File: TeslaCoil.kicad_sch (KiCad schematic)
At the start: 32 parts, among them J1 Screw_Terminal_01x03, J2 Screw_Terminal_01x02, Q1 Q_NIGBT_GCE, Q2 Q_NIGBT_GCE, Q3 Q_NIGBT_GCE, Q4 Q_NIGBT_GCE

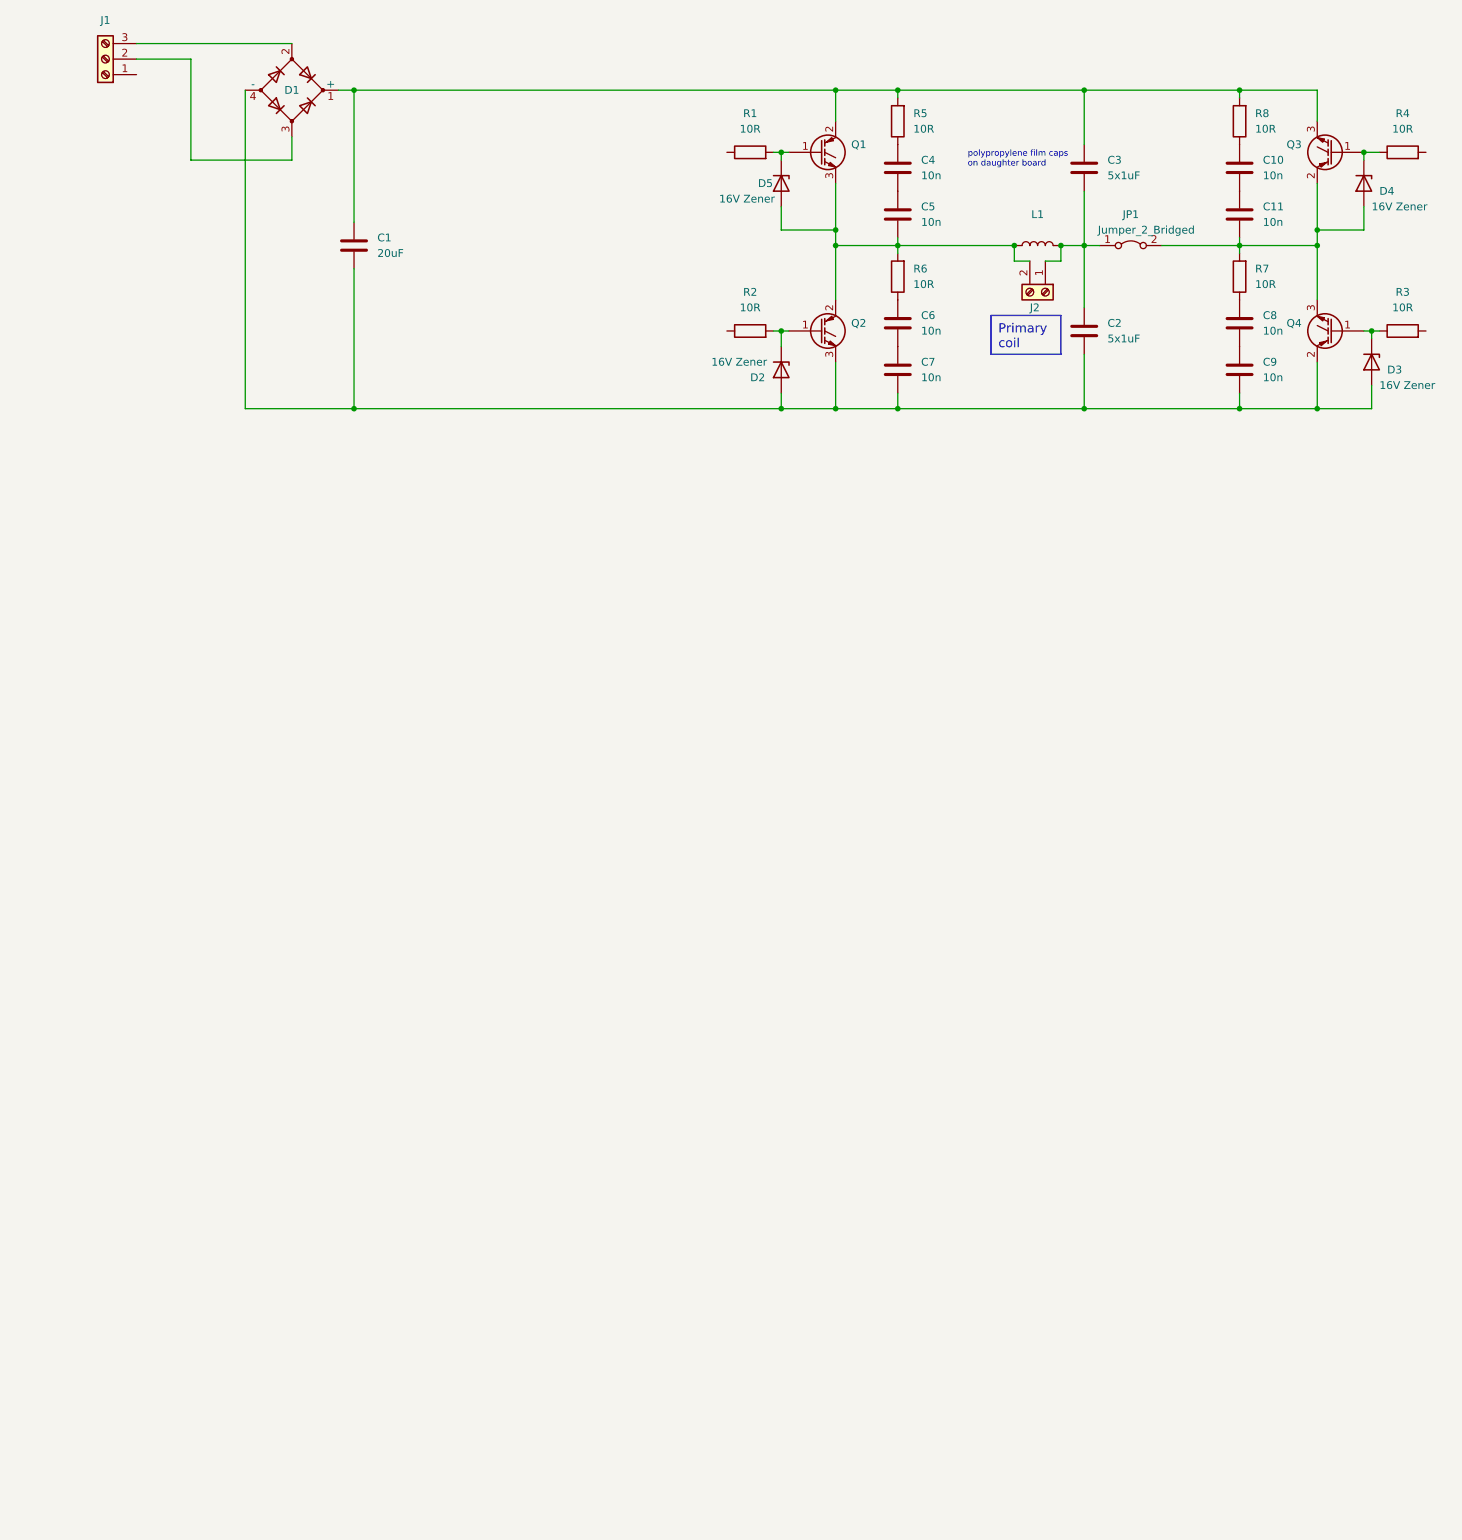
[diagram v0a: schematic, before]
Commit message: add gate driver
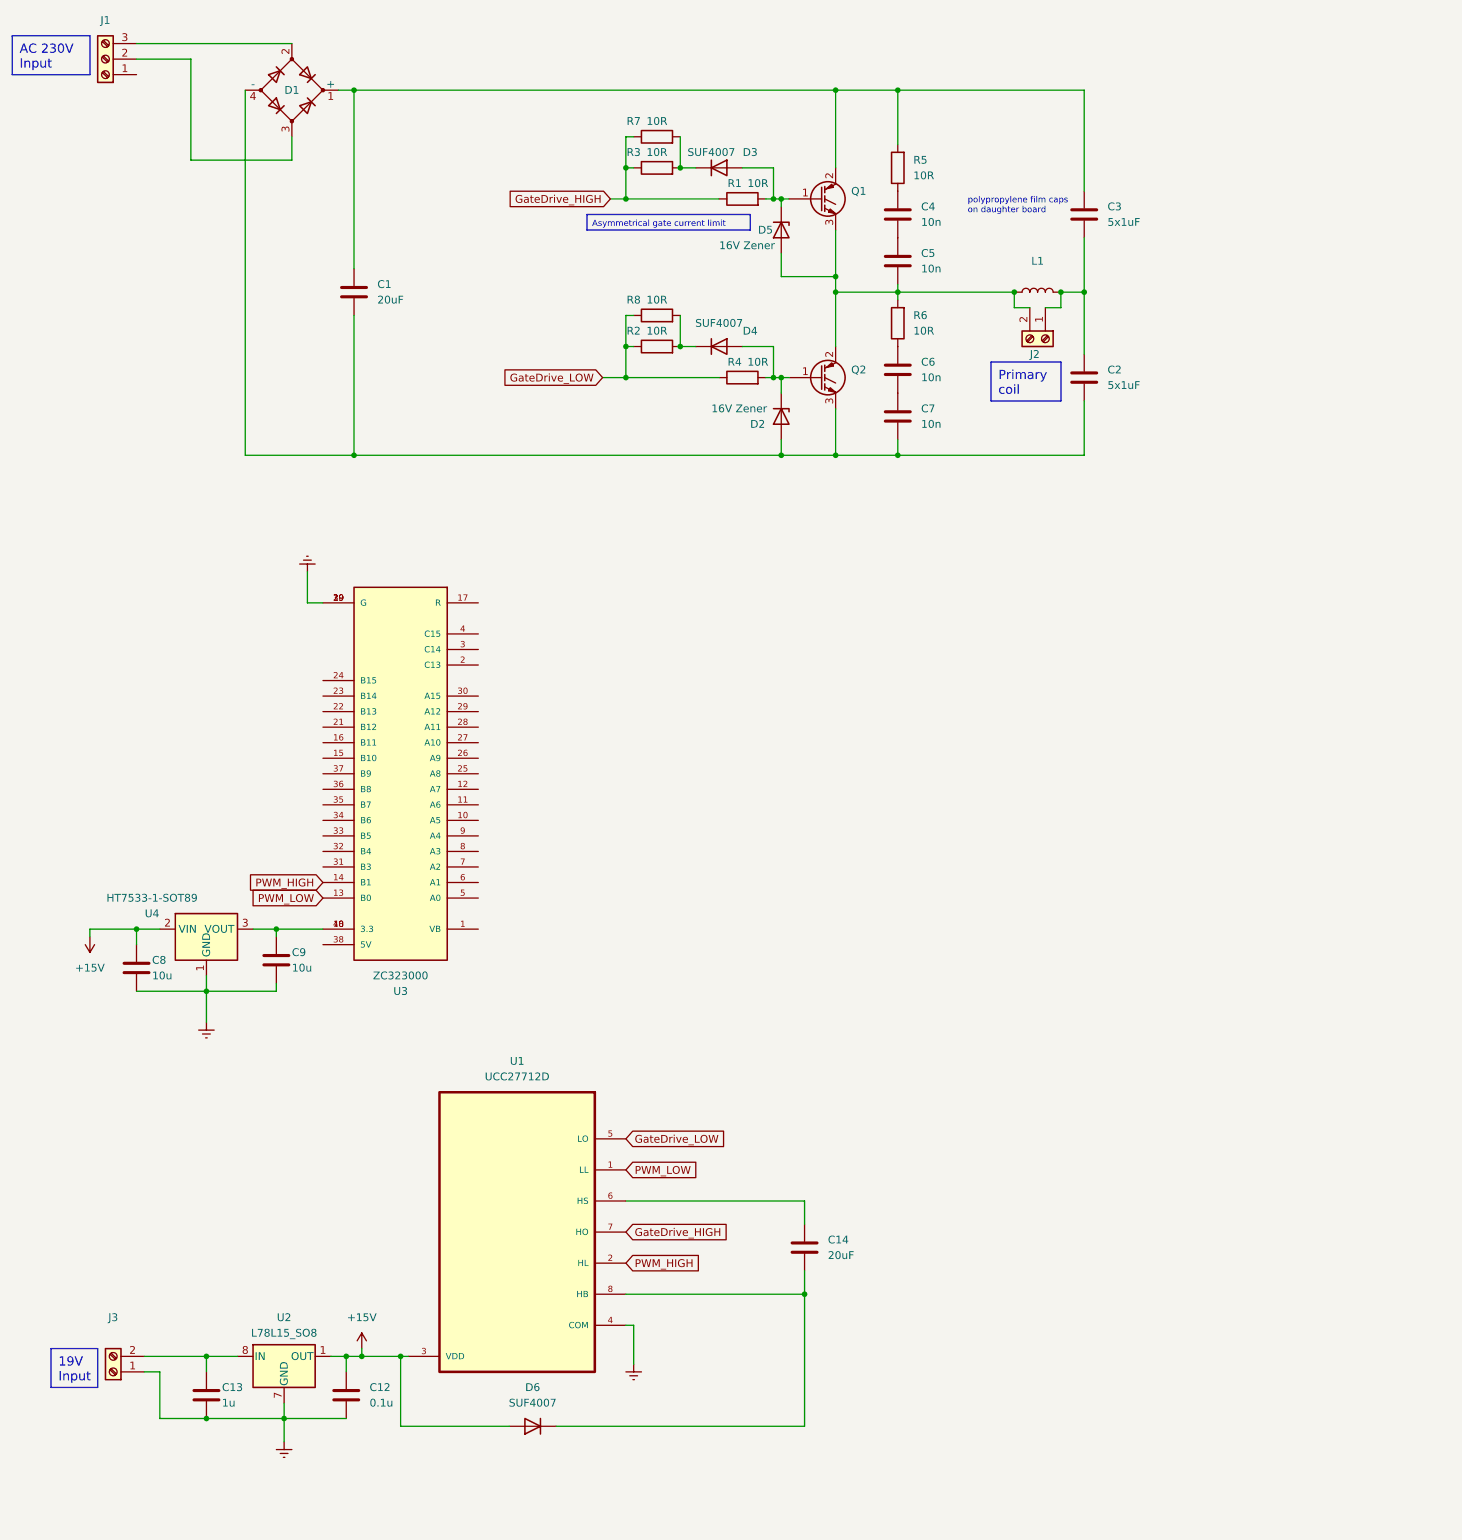
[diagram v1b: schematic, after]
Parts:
- removed C10, C11: 10n, symbol Device:C
- removed D3, D4: 16V Zener, symbol Device:D_Zener
- removed JP1: Jumper_2_Bridged, symbol Jumper:Jumper_2_Bridged
- removed Q3, Q4: Q_NIGBT_GCE, symbol Device:Q_NIGBT_GCE
- added C12: 0.1u, symbol Device:C
- added C13: 1u, symbol Device:C
- added C14: 20uF, symbol Device:C
- added D3, D4, D6: SUF4007, Diode_SMD:D_MELF_Handsoldering, symbol Diode:SM516
- added J3: Screw_Terminal_01x02, symbol Connector:Screw_Terminal_01x02
- added U1: UCC27712D, Snapeda:UCC27712D_SOIC127P599X175-8N, symbol Snapeda_kicad_sym:UCC27712D
- added U2: L78L15_SO8, Package_SO:SOIC-8_3.9x4.9mm_P1.27mm, symbol Regulator_Linear:L78L15_SO8
- added U3: ZC323000, Snapeda:ZC323000_MODULE_ZC323000, symbol Snapeda_kicad_sym:ZC323000
- added U4: HT7533-1-SOT89, Package_TO_SOT_SMD:SOT-89-3, symbol Regulator_Linear:HT75xx-1-SOT89
- C8, C9: value 10n -> 10u
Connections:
- net at C1.1, C3.1, D1.1 (+)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: no longer R8.2
- net at C1.2, C2.2, C7.2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: no longer C9.2
- net +15V: now reaches C8.1
- net +15V: now also C12.1, D6.2 (A), U1.3 (VDD), U2.1 (OUT), U4.2 (VIN); no longer R7.1
- net at C9.1: now also U3.18 (3.3), U3.40 (3.3), U4.3 (VOUT); no longer C8.2
- net GateDrive_HIGH: now reaches R3.1
- net GateDrive_HIGH: now also R1.1, R7.1, U1.7 (HO)
- net at R7.2: now also R3.2, D3.1 (K)
- net GateDrive_LOW: now reaches R2.1
- net GateDrive_LOW: now also R4.1, R8.1, U1.5 (LO)
- net at D2.1 (K), Q2.1 (G): now also R4.2, D4.2 (A); no longer R2.2
- net at D5.1 (K), Q1.1 (G), R1.2: now also D3.2 (A)
- new net: C13.1, J3.2 (Pin_2), U2.8 (IN)
- new net: D4.1 (K), R2.2, R8.2
- new net: C14.2, D6.1 (K), U1.8 (HB)
- new net: C14.1, U1.6 (HS)
- new net Earth: C12.2, C13.2, C8.2, C9.2, J3.1 (Pin_1), U1.4 (COM), U2.2 (GND), U2.3 (GND), U2.6 (GND), U2.7 (GND), U3.19 (G), U3.20 (G), U3.39 (G), U4.1 (GND)
- new net PWM_HIGH: U1.2 (HL), U3.14 (B1)
- new net PWM_LOW: U1.1 (LL), U3.13 (B0)
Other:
- moved on the sheet: C1, C2, C3, C4, C5, C6, C7, D2, D5, J2, L1, Q1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

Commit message: footprints
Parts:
- removed D1: D_Bridge_+AA-, symbol Device:D_Bridge_+AA-
- added D1: GBJ1008-BP, Snapeda:GBJ1008-BP_DIOB_GBJ1008-BP, symbol Snapeda_kicad_sym:GBJ1008-BP
- C1: footprint (none) -> Capacitor_THT:CP_Radial_D17.0mm_P7.50mm
- C12, C13, C14, C8, C9: footprint (none) -> Capacitor_SMD:C_0805_2012Metric_Pad1.18x1.45mm_HandSolder
- C2, C3: footprint (none) -> Capacitor_THT:C_Rect_L18.0mm_W5.0mm_P15.00mm_FKS3_FKP3
- C4, C5, C6, C7: footprint (none) -> Capacitor_THT:C_Rect_L13.0mm_W5.0mm_P10.00mm_FKS3_FKP3_MKS4
- D2, D5: footprint (none) -> Diode_SMD:D_0805_2012Metric
- J1: footprint (none) -> TerminalBlock_4Ucon:TerminalBlock_4Ucon_1x03_P3.50mm_Horizontal
- J2, J3: footprint (none) -> TerminalBlock_4Ucon:TerminalBlock_4Ucon_1x02_P3.50mm_Horizontal
- Q1, Q2: footprint (none) -> Package_TO_SOT_THT:TO-247-3_Vertical
- R1, R2, R3, R4, R7, R8: footprint (none) -> Resistor_SMD:R_0603_1608Metric_Pad0.98x0.95mm_HandSolder
- R5, R6: footprint (none) -> Resistor_THT:R_Axial_Power_L25.0mm_W9.0mm_P10.16mm_Vertical
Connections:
- net at C1.1, C3.1, Q1.2 (C)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: now also D1.4
- net at C1.2, C2.2, C7.2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: now also D1.1
- net at J1.2 (Pin_2): now also D1.3
- net at J1.3 (Pin_3): now also D1.2

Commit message: layout mockup
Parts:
- added D7, D8: SUF4007, Diode_SMD:D_MELF_Handsoldering, symbol Diode:SM516
- added L2: AS101, Snapeda:ASM-010_ASM-010, symbol Snapeda_kicad_sym:ASM-010
- added R10, R9: 100k, Resistor_THT:R_Axial_DIN0207_L6.3mm_D2.5mm_P7.62mm_Horizontal, symbol Device:R
- added R11: 1k, Resistor_THT:R_Axial_DIN0207_L6.3mm_D2.5mm_P7.62mm_Horizontal, symbol Device:R
- added SW1: SW_SPST, symbol Switch:SW_SPST
- added TP1: Current transformer wire, TestPoint:TestPoint_Bridge_Pitch7.62mm_Drill1.3mm, symbol Connector:TestPoint_2Pole
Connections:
- net Earth: now also D8.2 (A), L2.P$1
- net at C1.2, C2.2, C7.2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: now also R10.2
- net at D1.2: now also SW1.2 (B); no longer J1.3 (Pin_3)
- net at C1.1, C3.1, D1.4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: now also R9.1
- net +3.3V: now reaches C9.1, U3.18 (3.3), U3.40 (3.3), U4.3 (VOUT)
- net +3.3V: now also D7.1 (K)
- net at J2.1 (Pin_1), L1.2: now also TP1.1; no longer C2.1, C3.2
- net Current Sense: now reaches U3.6 (A1)
- net Current Sense: now also D7.2 (A), D8.1 (K), R11.2
- new net: L2.P$2, R11.1
- new net: C2.1, C3.2, R10.1, R9.2, TP1.2
- new net: J1.3 (Pin_3), SW1.1 (A)
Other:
- moved on the sheet: C2, C3, U3

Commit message: layout 2nd rev
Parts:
- removed C1: 20uF, Capacitor_THT:CP_Radial_D17.0mm_P7.50mm, symbol Device:C
- removed D2, D5: 16V Zener, Diode_SMD:D_0805_2012Metric, symbol Device:D_Zener
- removed D7, D8: SUF4007, Diode_SMD:D_MELF_Handsoldering, symbol Diode:SM516
- removed L2: AS101, Snapeda:ASM-010_ASM-010, symbol Snapeda_kicad_sym:ASM-010
- removed TP1: Current transformer wire, TestPoint:TestPoint_Bridge_Pitch7.62mm_Drill1.3mm, symbol Connector:TestPoint_2Pole
- removed U2: L78L15_SO8, Package_SO:SOIC-8_3.9x4.9mm_P1.27mm, symbol Regulator_Linear:L78L15_SO8
- added C1, C10, C11, C15: 220uF, Capacitor_THT:CP_Radial_D22.0mm_P10.00mm_SnapIn, symbol Device:C_Polarized_US
- added C16: 4x100nF, Capacitor_SMD:C_0603_1608Metric, symbol Device:C
- added D2, D5, D7: LED, LED_SMD:LED_0805_2012Metric, symbol Device:LED
- added J4: MCSP-Q-08-A-SG-T_R, Samacsys:MCSPQ08ASGTR, symbol Samacsys_kicad_sym:MCSP-Q-08-A-SG-T_R
- added JP1, JP2, JP3, JP4, JP5, JP6, JP7, JP8: Solder Jumper, Jumper:SolderJumper-2_P1.3mm_Open_TrianglePad1.0x1.5mm, symbol Jumper:SolderJumper_2_Open
- added R12, R14, R15, R18, R19: 1k, Resistor_SMD:R_0603_1608Metric_Pad0.98x0.95mm_HandSolder, symbol Device:R
- added R13: 10k, Resistor_SMD:R_0603_1608Metric_Pad0.98x0.95mm_HandSolder, symbol Device:R
- added R16, R17: 10R, Resistor_SMD:R_0603_1608Metric_Pad0.98x0.95mm_HandSolder, symbol Device:R
- added RV1: 10k pot, Snapeda:potentiometer, symbol Device:R_Potentiometer
- added T1: Gate drive transformer, Transformer_THT:Transformer_Toroid_Tapped_Horizontal_D10.5mm_Amidon-T37, symbol Device:Transformer_1P_2S
- added U2: LM317_TO-220, Package_TO_SOT_THT:TO-220-3_Vertical, symbol Regulator_Linear:LM317_TO-220
- C12: value 0.1u -> 100nF; footprint Capacitor_SMD:C_0805_2012Metric_Pad1.18x1.45mm_HandSolder -> Capacitor_SMD:C_0603_1608Metric
- C13: value 1u -> 100nF; footprint Capacitor_SMD:C_0805_2012Metric_Pad1.18x1.45mm_HandSolder -> Capacitor_SMD:C_0603_1608Metric
- C14: value 20uF -> 100nF; footprint Capacitor_SMD:C_0805_2012Metric_Pad1.18x1.45mm_HandSolder -> Capacitor_SMD:C_0603_1608Metric
- R11: footprint Resistor_THT:R_Axial_DIN0207_L6.3mm_D2.5mm_P7.62mm_Horizontal -> Resistor_SMD:R_0603_1608Metric_Pad0.98x0.95mm_HandSolder
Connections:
- net +15V: now also D7.2 (A), R12.2, U2.2 (VO); no longer C12.1, D6.2 (A), U1.3 (VDD)
- net +3.3V: now also J4.4 (VDD), RV1.3
- net Earth: now also R11.1, J4.6 (VSS), J4.MP1, J4.MP2, J4.MP3, J4.MP4, JP7.2 (B), JP8.1 (A), R14.1, R15.1, R19.1, RV1.1; no longer C12.2, C13.2
- net PWM_HIGH: now also U3.13 (B0), R16.2; no longer U1.2 (HL), U3.14 (B1)
- net PWM_LOW: now also U3.14 (B1), R17.2; no longer U1.1 (LL), U3.13 (B0)
- net at J3.2 (Pin_2): now also U2.3 (VI); no longer C13.1
- net Bridge_Low: now reaches C2.2, C7.2, D1.1, Q2.3 (E), R10.2
- net Bridge_Low: now also C10.2, C15.2, JP8.2 (B), T1.6 (SD)
- net at C3.1, D1.4, Q1.2 (C)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: now also C1.1, C11.1
- net Bridge_Midpoint: now reaches C5.2, J2.2 (Pin_2), L1.1, Q1.3 (E), Q2.2 (C), R6.2
- net Bridge_Midpoint: now also JP6.2 (B), T1.4 (SB)
- net at C14.2, D6.1 (K), U1.8 (HB): now also C12.2, C13.2, C16.2
- net at C14.1, U1.6 (HS): now also C12.1, C13.1, C16.1, JP6.1 (A), JP7.1 (A)
- net at J2.1 (Pin_1), L1.2: now also C2.1, C3.2, R10.1, R9.2, C1.2, C10.1, C11.2, C15.1
- net at U3.10 (A5): now also J4.5 (CLX)
- net at U3.11 (A6): now also J4.7 (DAT0)
- net at U3.12 (A7): now also J4.3 (CMD)
- net at U3.15 (B10): now also D2.2 (A)
- net at U3.16 (B11): now also D5.2 (A)
- net at U3.9 (A4): now also J4.2 (CD/DAT3)
- net Current Sense: no longer names the net of U3.6 (A1)
- net Current Sense: now also RV1.2; no longer R11.2
- net GateDrive_HIGH: no longer names the net of R7.1, U1.7 (HO)
- net GateDrive_HIGH: now also R4.1, R8.1; no longer R1.1, R3.1
- net GateDrive_LOW: no longer names the net of R2.1, U1.5 (LO)
- net GateDrive_LOW: now also R1.1, R3.1; no longer R4.1, R8.1
- new net: R13.1, R14.2
- new net: R12.1, R13.2, U2.1 (ADJ)
- new net: R18.1, R19.2
- new net: D7.1 (K), R18.2
- new net: D3.1 (K), R1.2, R2.2
- new net: R17.1, U1.1 (LL)
- new net: JP1.1 (A), T1.3 (SA)
- new net: JP1.2 (B), JP5.2 (B), Q1.1 (G)
- new net: JP2.2 (B), JP4.2 (B), Q2.1 (G)
- new net: D2.1 (K), R15.2
- new net: D6.2 (A), U1.3 (VDD)
- new net: R16.1, U1.2 (HL)
- new net: JP3.2 (B), T1.1 (AA)
- new net: JP2.1 (A), T1.5 (SC)
- new net: D5.1 (K), R11.2
- new net: D4.1 (K), R4.2, R7.2
- new net DriverOut_HIGH: D4.2 (A), JP3.1 (A), JP5.1 (A), R8.2
- new net DriverOut_LOW: D3.2 (A), JP4.1 (A), R3.2, T1.2 (AB)
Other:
- moved on the sheet: C14, C8, C9, D6, J2, L1, U1, U3, U4

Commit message: amogus
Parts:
- T1: value Gate drive transformer -> GDT
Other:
- moved on the sheet: D2, D5, J4, R11, R15, RV1, U3

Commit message: final v1
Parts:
- SW1: footprint (none) -> Snapeda:Rocker switch
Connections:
- net Earth: now also J1.1 (Pin_1)
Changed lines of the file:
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@@
+    )
+  )
+  (symbol (lib_id "power:Earth") (at 34.29 44.45 0) (unit 1)
+    (in_bom yes) (on_board yes) (dnp no) (fields_autoplaced)
+    (property "Reference" "#PWR017" (at 34.29 50.8 0)
+      (effects (font (size 1.27 1.27)) hide)
+    )
+    (property "Value" "Earth" (at 34.29 48.26 0)
+      (effects (font (size 1.27 1.27)) hide)
+    )
+    (property "Footprint" "" (at 34.29 44.45 0)
+      (effects (font (size 1.27 1.27)) hide)
+    )
+    (property "Datasheet" "~" (at 34.29 44.45 0)
+      (effects (font (size 1.27 1.27)) hide)
+    )
+    (pin "1")
+    (instances
+      (project "TeslaCoil"
+        (path "/d208d53a-537f-4313-a183-63c8e419e433"
+          (reference "#PWR017") (unit 1)
+        )
+      )
     )
   )
@@
   )
   (symbol (lib_id "Switch:SW_SPST") (at 45.72 39.37 0) (unit 1)
-    (in_bom yes) (on_board no) (dnp no)
+    (in_bom yes) (on_board yes) (dnp no)
     (property "Reference" "SW1" (at 46.99 35.56 0)
       (effects (font (size 1.27 1.27)))
@@
       (effects (font (size 1.27 1.27)) hide)
     )
-    (property "Footprint" "" (at 45.72 39.37 0)
-      (effects (font (size 1.27 1.27)) hide)
-    )
+    (property "Footprint" "Snapeda:Rocker switch" (at 45.72 39.37 0)
+      (effects (font (size 1.27 1.27)) hide)
+    )
